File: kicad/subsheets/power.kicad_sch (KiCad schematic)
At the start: 12 parts, among them U1 AP61300Z6, U7 AP61300Z6

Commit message: Annotations
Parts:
- renumbered C4 to C1, C58 to C2, C1 to C3, C2 to C4, L7 to L1, L1 to L2, R37 to R10, R38 to R11, R29 to R8, R36 to R9, U7 to U1, U1 to U2
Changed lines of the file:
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@@
 		(on_board yes)
 		(dnp no)
-		(property "Reference" "C1"
+		(property "Reference" "C3"
 			(at 41.148 64.516 0)
 			(effects
@@
 			(project "srad-camera"
 				(path "/da62c771-e8c9-451f-8df1-ec995aadcb11/7609dbdd-9f9c-4b95-995a-5c84c03ab6a6"
-					(reference "C1")
+					(reference "C3")
 					(unit 1)
 				)
@@
 		(dnp no)
 		(fields_autoplaced yes)
-		(property "Reference" "R37"
+		(property "Reference" "R10"
 			(at 81.28 64.7699 0)
 			(effects
@@
 			(project "srad-camera"
 				(path "/da62c771-e8c9-451f-8df1-ec995aadcb11/7609dbdd-9f9c-4b95-995a-5c84c03ab6a6"
-					(reference "R37")
+					(reference "R10")
 					(unit 1)
 				)
@@
 		(on_board yes)
 		(dnp no)
-		(property "Reference" "C58"
+		(property "Reference" "C2"
 			(at 89.662 32.766 0)
 			(effects
@@
 			(project "srad-camera"
 				(path "/da62c771-e8c9-451f-8df1-ec995aadcb11/7609dbdd-9f9c-4b95-995a-5c84c03ab6a6"
-					(reference "C58")
+					(reference "C2")
 					(unit 1)
 				)
@@
 		(dnp no)
 		(fields_autoplaced yes)
-		(property "Reference" "R29"
+		(property "Reference" "R8"
 			(at 81.28 29.2099 0)
 			(effects
@@
 			(project "srad-camera"
 				(path "/da62c771-e8c9-451f-8df1-ec995aadcb11/7609dbdd-9f9c-4b95-995a-5c84c03ab6a6"
-					(reference "R29")
+					(reference "R8")
 					(unit 1)
 				)
@@
 		(on_board yes)
 		(dnp no)
-		(property "Reference" "L1"
+		(property "Reference" "L2"
 			(at 72.136 55.88 90)
 			(effects
@@
 			(project "srad-camera"
 				(path "/da62c771-e8c9-451f-8df1-ec995aadcb11/7609dbdd-9f9c-4b95-995a-5c84c03ab6a6"
-					(reference "L1")
+					(reference "L2")
 					(unit 1)
 				)
@@
 		(on_board yes)
 		(dnp no)
-		(property "Reference" "#PWR035"
+		(property "Reference" "#PWR014"
 			(at 58.42 49.53 0)
 			(effects
@@
 			(project "srad-camera"
 				(path "/da62c771-e8c9-451f-8df1-ec995aadcb11/7609dbdd-9f9c-4b95-995a-5c84c03ab6a6"
-					(reference "#PWR035")
+					(reference "#PWR014")
 					(unit 1)
 				)
@@
 		(on_board yes)
 		(dnp no)
-		(property "Reference" "U7"
+		(property "Reference" "U1"
 			(at 58.42 17.526 0)
 			(effects
@@
 			(project "srad-camera"
 				(path "/da62c771-e8c9-451f-8df1-ec995aadcb11/7609dbdd-9f9c-4b95-995a-5c84c03ab6a6"
-					(reference "U7")
+					(reference "U1")
 					(unit 1)
 				)
@@
 		(on_board yes)
 		(dnp no)
-		(property "Reference" "#PWR02"
+		(property "Reference" "#PWR015"
 			(at 58.42 85.09 0)
 			(effects
@@
 			(project "srad-camera"
 				(path "/da62c771-e8c9-451f-8df1-ec995aadcb11/7609dbdd-9f9c-4b95-995a-5c84c03ab6a6"
-					(reference "#PWR02")
+					(reference "#PWR015")
 					(unit 1)
 				)
@@
 		(dnp no)
 		(fields_autoplaced yes)
-		(property "Reference" "R36"
+		(property "Reference" "R9"
 			(at 81.28 36.8299 0)
 			(effects
@@
 			(project "srad-camera"
 				(path "/da62c771-e8c9-451f-8df1-ec995aadcb11/7609dbdd-9f9c-4b95-995a-5c84c03ab6a6"
-					(reference "R36")
+					(reference "R9")
 					(unit 1)
 				)
@@
 		(on_board yes)
 		(dnp no)
-		(property "Reference" "L7"
+		(property "Reference" "L1"
 			(at 72.136 20.32 90)
 			(effects
@@
 			(project "srad-camera"
 				(path "/da62c771-e8c9-451f-8df1-ec995aadcb11/7609dbdd-9f9c-4b95-995a-5c84c03ab6a6"
-					(reference "L7")
+					(reference "L1")
 					(unit 1)
 				)
@@
 		(on_board yes)
 		(dnp no)
-		(property "Reference" "U1"
+		(property "Reference" "U2"
 			(at 58.42 53.086 0)
 			(effects
@@
 			(project "srad-camera"
 				(path "/da62c771-e8c9-451f-8df1-ec995aadcb11/7609dbdd-9f9c-4b95-995a-5c84c03ab6a6"
-					(reference "U1")
+					(reference "U2")
 					(unit 1)
 				)
@@
 		(dnp no)
 		(fields_autoplaced yes)
-		(property "Reference" "R38"
+		(property "Reference" "R11"
 			(at 81.28 72.3899 0)
 			(effects
@@
 			(project "srad-camera"
 				(path "/da62c771-e8c9-451f-8df1-ec995aadcb11/7609dbdd-9f9c-4b95-995a-5c84c03ab6a6"
-					(reference "R38")
+					(reference "R11")
 					(unit 1)
 				)
@@
 		(on_board yes)
 		(dnp no)
-		(property "Reference" "C4"
+		(property "Reference" "C1"
 			(at 41.148 28.956 0)
 			(effects
@@
 			(project "srad-camera"
 				(path "/da62c771-e8c9-451f-8df1-ec995aadcb11/7609dbdd-9f9c-4b95-995a-5c84c03ab6a6"
-					(reference "C4")
+					(reference "C1")
 					(unit 1)
 				)
@@
 		(on_board yes)
 		(dnp no)
-		(property "Reference" "C2"
+		(property "Reference" "C4"
 			(at 89.662 68.326 0)
 			(effects
@@
 			(project "srad-camera"
 				(path "/da62c771-e8c9-451f-8df1-ec995aadcb11/7609dbdd-9f9c-4b95-995a-5c84c03ab6a6"
-					(reference "C2")
-					(unit 1)
-				)
+					(reference "C4")
+					(unit 1)
+				)

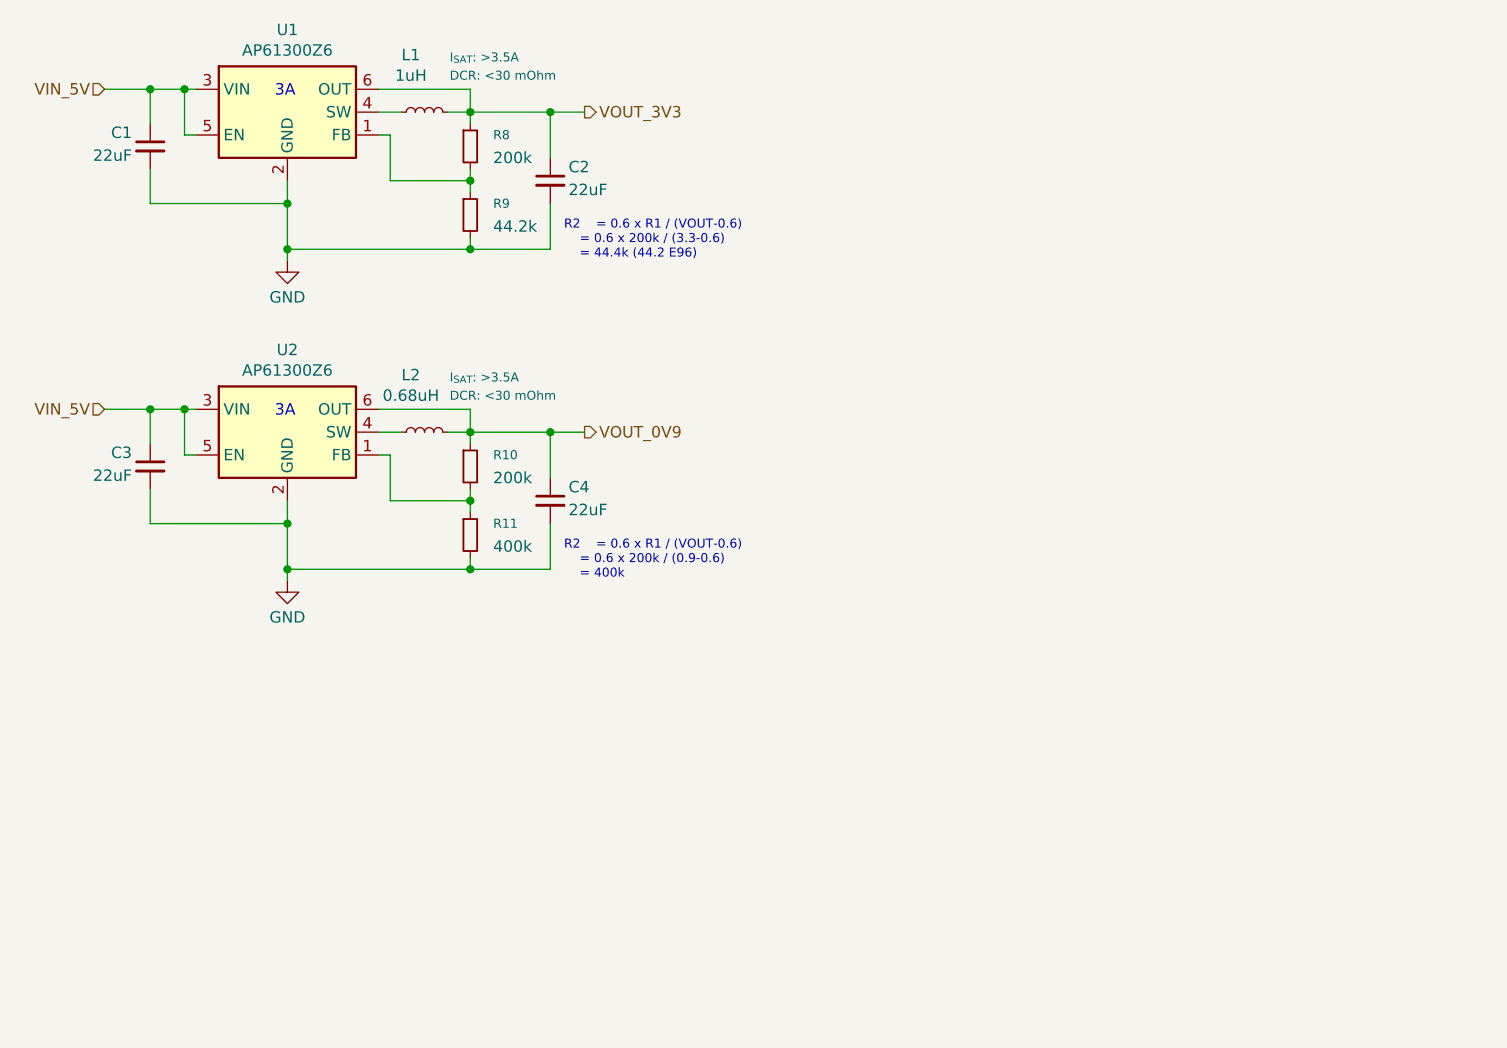
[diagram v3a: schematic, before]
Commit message: Change all sheets to A4, name sheets, split RK3566 into hierarchy
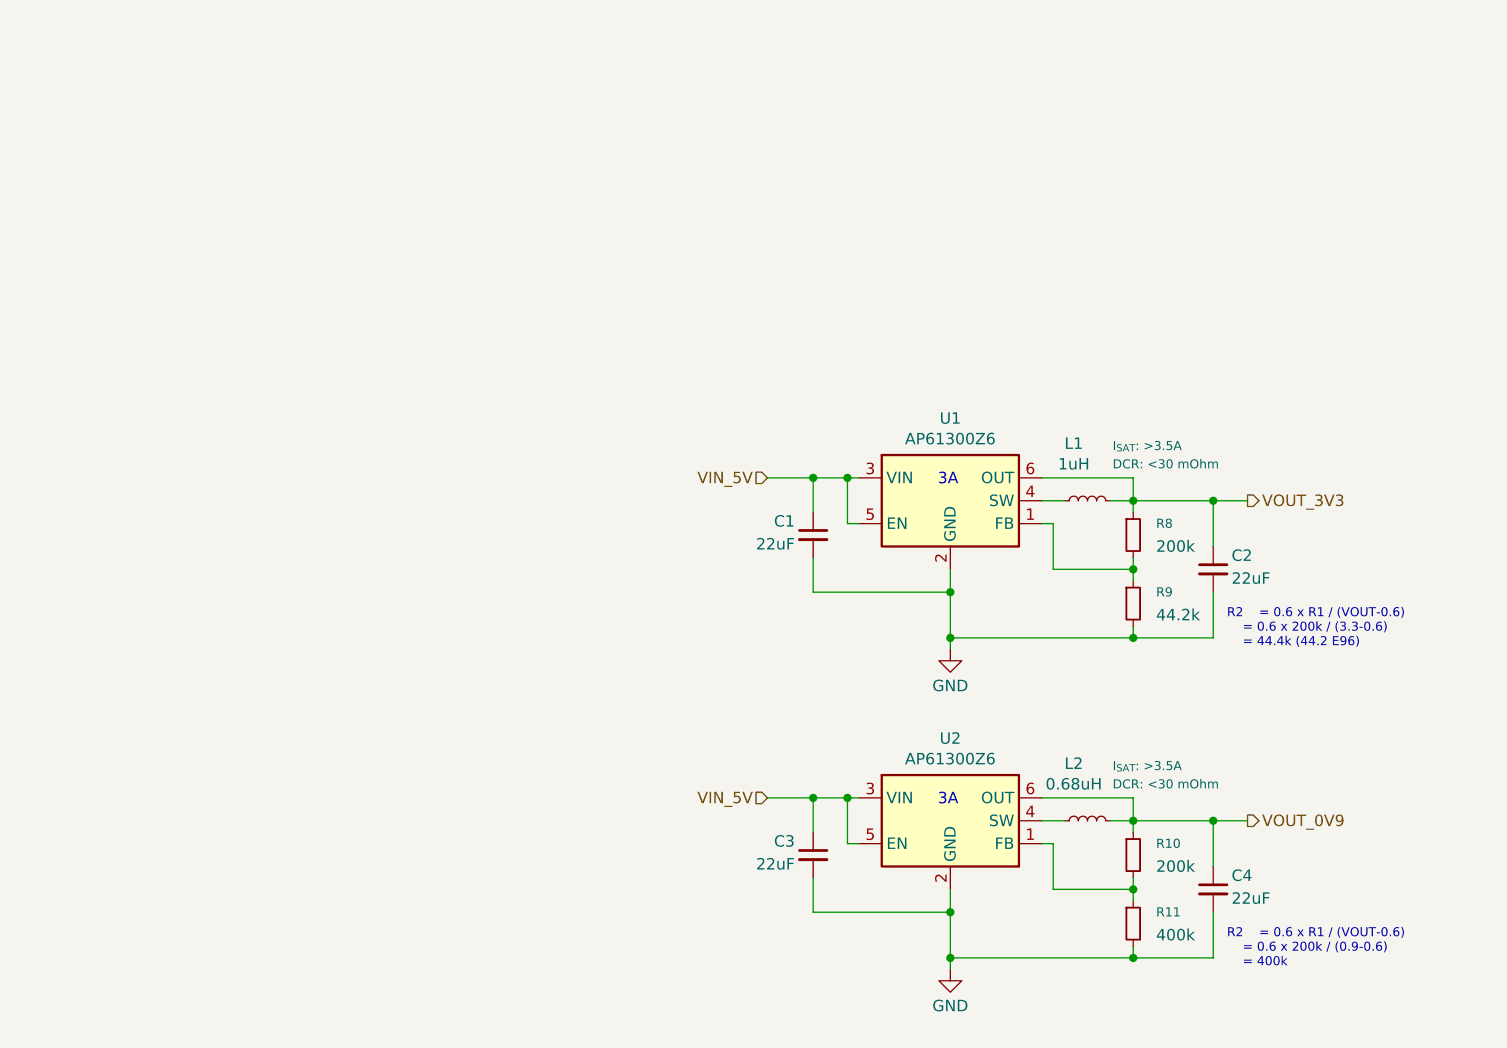
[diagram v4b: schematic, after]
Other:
- title: (none) -> Buck Converters
- moved on the sheet: C1, C2, C3, C4, L1, L2, R10, R11, R8, R9, U1, U2

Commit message: Mark as R1.0
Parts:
- renumbered C1 to C2, C2 to C3, C3 to C4, C4 to C5
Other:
- company: (none) -> UVic Rocketry
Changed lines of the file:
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@@
 	(title_block
 		(title "Buck Converters")
+		(date "2025-11-23")
+		(rev "1.0")
+		(company "UVic Rocketry")
+		(comment 1 "Author: Eric Handley")
 	)
 	(text "R2	= 0.6 x R1 / (VOUT-0.6)\n	= 0.6 x 200k / (0.9-0.6) \n	= 400k"
@@
 		(on_board yes)
 		(dnp no)
-		(property "Reference" "C3"
+		(property "Reference" "C4"
 			(at 114.808 107.696 0)
 			(effects
@@
 			(project "srad-camera"
 				(path "/da62c771-e8c9-451f-8df1-ec995aadcb11/7609dbdd-9f9c-4b95-995a-5c84c03ab6a6"
-					(reference "C3")
+					(reference "C4")
 					(unit 1)
 				)
@@
 		(on_board yes)
 		(dnp no)
-		(property "Reference" "C2"
+		(property "Reference" "C3"
 			(at 163.322 75.946 0)
 			(effects
@@
 			(project "srad-camera"
 				(path "/da62c771-e8c9-451f-8df1-ec995aadcb11/7609dbdd-9f9c-4b95-995a-5c84c03ab6a6"
-					(reference "C2")
+					(reference "C3")
 					(unit 1)
 				)
@@
 		(on_board yes)
 		(dnp no)
-		(property "Reference" "#PWR017"
+		(property "Reference" "#PWR019"
 			(at 132.08 92.71 0)
 			(effects
@@
 			(project "srad-camera"
 				(path "/da62c771-e8c9-451f-8df1-ec995aadcb11/7609dbdd-9f9c-4b95-995a-5c84c03ab6a6"
-					(reference "#PWR017")
+					(reference "#PWR019")
 					(unit 1)
 				)
@@
 		(on_board yes)
 		(dnp no)
-		(property "Reference" "#PWR018"
+		(property "Reference" "#PWR020"
 			(at 132.08 128.27 0)
 			(effects
@@
 			(project "srad-camera"
 				(path "/da62c771-e8c9-451f-8df1-ec995aadcb11/7609dbdd-9f9c-4b95-995a-5c84c03ab6a6"
-					(reference "#PWR018")
+					(reference "#PWR020")
 					(unit 1)
 				)
@@
 		(on_board yes)
 		(dnp no)
-		(property "Reference" "C1"
+		(property "Reference" "C2"
 			(at 114.808 72.136 0)
 			(effects
@@
 			(project "srad-camera"
 				(path "/da62c771-e8c9-451f-8df1-ec995aadcb11/7609dbdd-9f9c-4b95-995a-5c84c03ab6a6"
-					(reference "C1")
+					(reference "C2")
 					(unit 1)
 				)
@@
 		(on_board yes)
 		(dnp no)
-		(property "Reference" "C4"
+		(property "Reference" "C5"
 			(at 163.322 111.506 0)
 			(effects
@@
 			(project "srad-camera"
 				(path "/da62c771-e8c9-451f-8df1-ec995aadcb11/7609dbdd-9f9c-4b95-995a-5c84c03ab6a6"
-					(reference "C4")
+					(reference "C5")
 					(unit 1)
 				)

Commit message: Start on PCB design
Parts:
- removed R11: 400k, symbol Device:R_Small
- added R10: 22k, Resistor_SMD:R_0402_1005Metric, symbol Device:R_Small
- added R12, R13: 200k, Resistor_SMD:R_0402_1005Metric, symbol Device:R_Small
- C2, C3, C4, C5: footprint (none) -> Capacitor_SMD:C_1206_3216Metric; LCSC PART NAME (none) -> C12891
- L1: footprint (none) -> Inductor_SMD:L_0805_2012Metric; LCSC PART NAME (none) -> C1042
- L2: value 0.68uH -> 680nH; footprint (none) -> Inductor_SMD:L_0603_1608Metric; LCSC PART NAME (none) -> C55546
- R11: renamed from R10; footprint (none) -> Resistor_SMD:R_0402_1005Metric; LCSC PART NAME (none) -> C25764
- R8: footprint (none) -> Resistor_SMD:R_0402_1005Metric; LCSC PART NAME (none) -> C25764
- R9: value 44.2k -> 22k; footprint (none) -> Resistor_SMD:R_0402_1005Metric; LCSC PART NAME (none) -> C25768
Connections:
- net GND: now also R10.2, R13.2; no longer R9.2
- net at R11.2, U2.1 (FB): now also R12.1
- new net: R12.2, R13.1
- new net: R10.1, R9.2
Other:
- moved on the sheet: R9
